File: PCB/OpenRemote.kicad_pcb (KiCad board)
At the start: 2 copper layers, 192.4 x 50 mm, 187 parts, among them J1 USB_C_Receptacle_USB2.0, J2 Conn_01x50, J3 JST_PH_B2B-PH, J4 2.54x2 Header, J5 Micro_SD_Card, Q1 DMG2301L, Q2 MBT3904DW1, Q3 DMG2301L, Q4 DMG2301L, Q5 DMG2301L, Q6 FS8205A, Q7 DMG2301L, U1 DW01A, U10 APX803S, U11 TP4056, U12 TCA8418, U2 XC6220B331, U3 CH340C, U4 USBLC6-2P6, U5 LIS3DHTR, U6 TSSP77038, U7 ESP32-S3-WROOM-1-N16R8, U8 AP2112K-3.3, U9 MAX17048G

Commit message: Start Rev 6 Schematic
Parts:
- D2: footprint omoteLib:LED_5mm_Side_Mount -> OpenRemoteLib:LED_5mm_Side_Mount
- J1: footprint omoteLib:USB_C_Receptacle_HRO_TYPE-C-31-M-12 -> OpenRemoteLib:USB_C_Receptacle_HRO_TYPE-C-31-M-12
- J2: footprint omoteLib:TFT_2.83IN_240X320_50PIN -> OpenRemoteLib:TFT_2.83IN_240X320_50PIN
- J3: footprint omoteLib:JST_PH_B2B-PH-SM4-TB_1x02-1MP_P2.00mm_Vertical -> OpenRemoteLib:JST_PH_B2B-PH-SM4-TB_1x02-1MP_P2.00mm_Vertical
- J5: footprint omoteLib:MicroSD Slot TF-01A -> OpenRemoteLib:MicroSD Slot TF-01A
- U5: footprint omoteLib:XDCR_LIS3DHTR -> OpenRemoteLib:XDCR_LIS3DHTR
- U6: footprint omoteLib:Heimdall vertical -> OpenRemoteLib:Heimdall vertical

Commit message: Prepared to place mic on PCB
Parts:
- added MIC1: MS3625 Module, OpenRemoteLib:MS3625_Module_Back_Mount_SMD, B.Cu at (185.0, 171.0)
- added R45: 4k7, Resistor_SMD:R_0603_1608Metric, F.Cu at (195.1, 164.3)
- added R46: 4k7, Resistor_SMD:R_0603_1608Metric, F.Cu at (195.1, 166.8)
- added R47: 4k7, Resistor_SMD:R_0603_1608Metric, F.Cu at (195.1, 169.3)
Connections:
- net Net-(D3-A) renamed MIC_VDD

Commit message: Placed microphone on rear of PCB
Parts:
- MIC1: value MS3625 Module -> Mic Module; moved to F.Cu
- moved MIC1 81.1 mm to (142.5, 102.0), turned to 90 degrees
- moved R47 76.7 mm to (144.0, 112.0), turned to 90 degrees
- moved R46 75.9 mm to (142.5, 112.0), turned to -90 degrees
- moved R45 75.2 mm to (141.0, 112.0), turned to 90 degrees
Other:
- board text added: "GND"

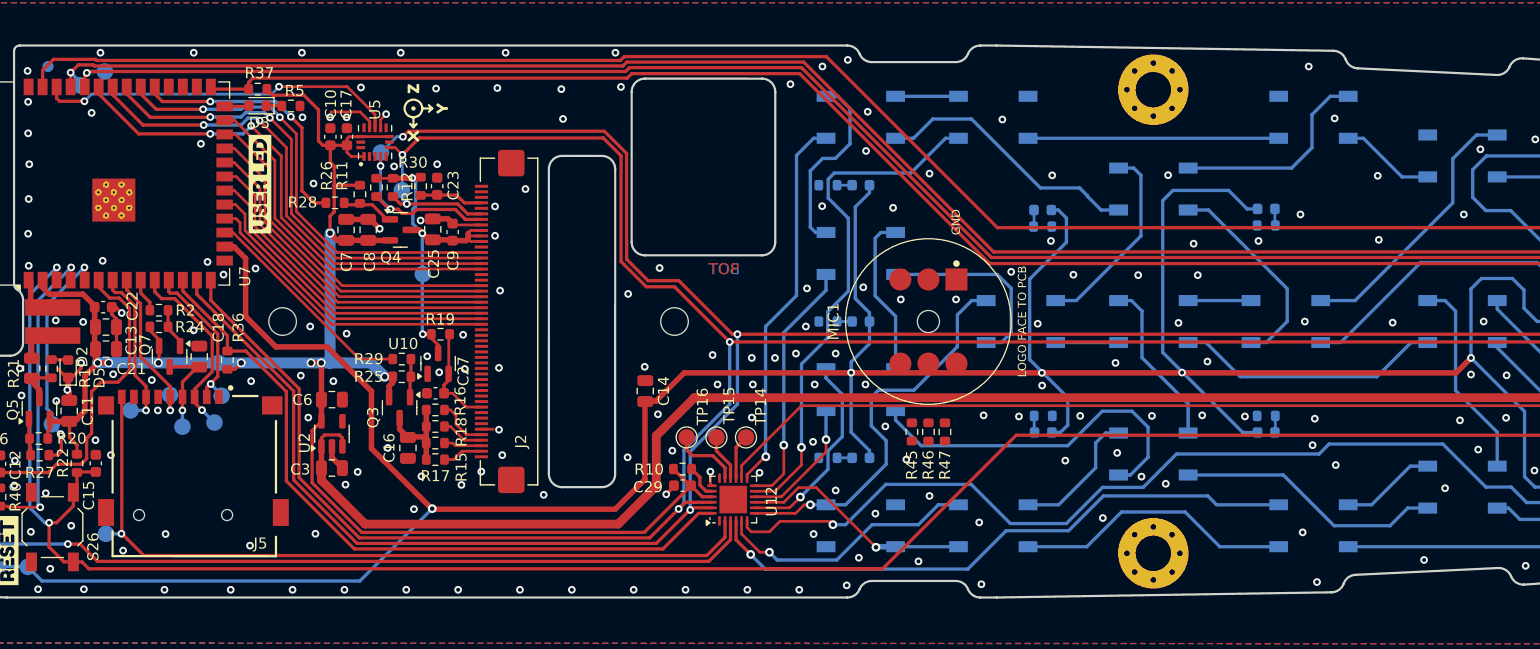
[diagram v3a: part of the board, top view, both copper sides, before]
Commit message: Routed microphone traces
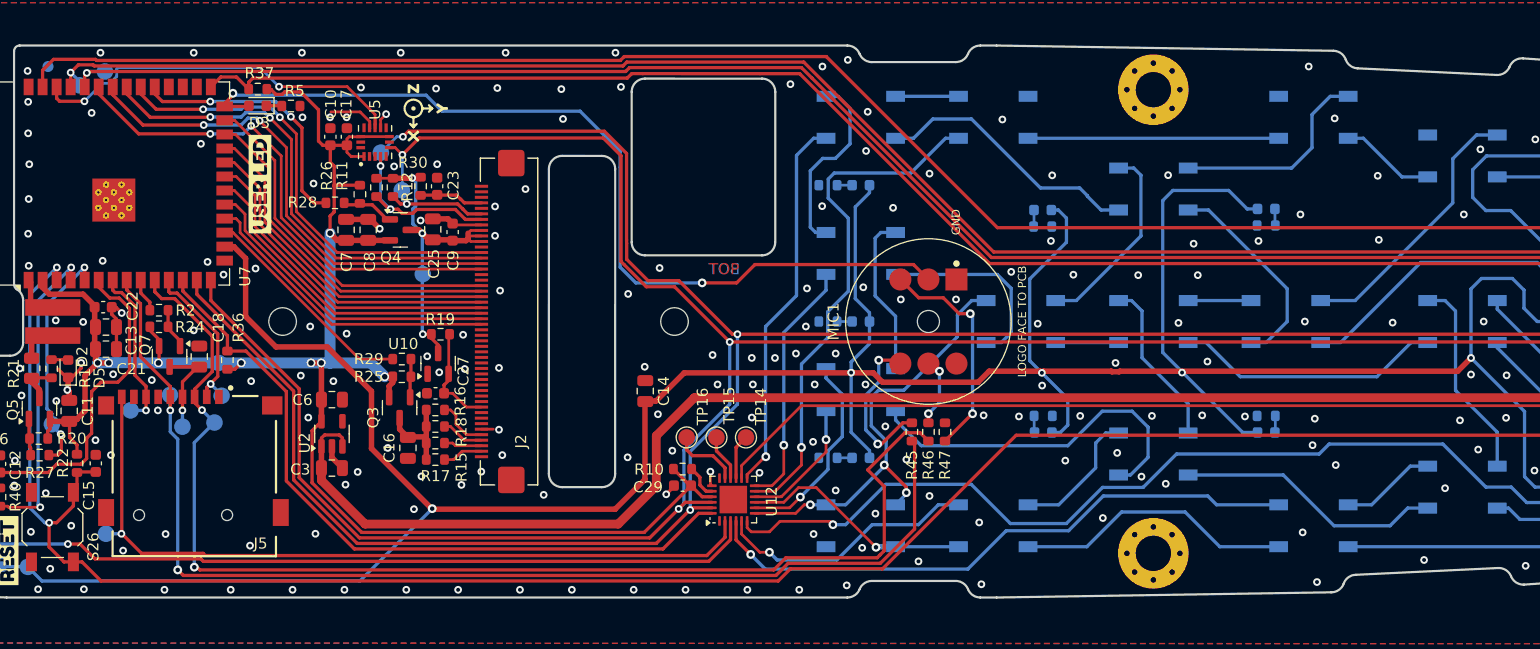
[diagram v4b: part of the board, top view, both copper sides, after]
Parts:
- turned R45 to -90 degrees
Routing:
- net SD_MOSI: track 17.2 -> 109.8 mm, vias 1 -> 2
- net SD_SCK: track 14.8 -> 106.3 mm, vias 1 -> 2
- net MIC_VDD: track 2.23 -> 81.2 mm, vias 0 -> 2
- net Net-(MIC1-SD): track 0.00 -> 20.3 mm, vias 0 -> 2
- net Net-(MIC1-SCK): track 0.00 -> 15.6 mm, vias 0 -> 2
- net Net-(MIC1-WS): track 0.00 -> 6.38 mm, vias 0 -> 2
- net SW_D: track 73.8 -> 78.1 mm, vias 1 -> 3
- net ACC_INT: track 33.3 -> 35.2 mm
- net ESP_EN: track 209.2 -> 210.1 mm
- net SW_BL: track 343.4 -> 344.3 mm
- net IO0: track 159.3 -> 160.1 mm
